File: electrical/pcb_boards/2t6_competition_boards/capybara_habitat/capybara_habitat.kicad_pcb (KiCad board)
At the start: 2 copper layers, 137.3 x 78 mm, 100 parts, among them J1 Barrel_Jack, J10 leds_sw, J11 monitor2_power, J12 2nd_disp_sw, J13 spare_usb_2nd_disp_pwr, J14 aud_sig_out_a, J15 aud_sig_out_b, J16 aud_sig_in, J18 spkrs_sw, J2 charger_buck_in, J3 vbatt, J4 Raspberry_Pi_4, J5 Raspberry_Pi_4, J7 1st_disp_sw, J8 leds_power, J9 monitor1_power, U1 Adafruit_INA219, U2 Adafruit_INA219, U3 LTC3114IFE-1_TRPBF, U4 LT8610ABEMSE-5-TRPBF, U5 TPS22810DBV, U6 TPS22810DBV, U7 TPS22810DBV, U8 TPS22810DBV, U9 PAM8406D

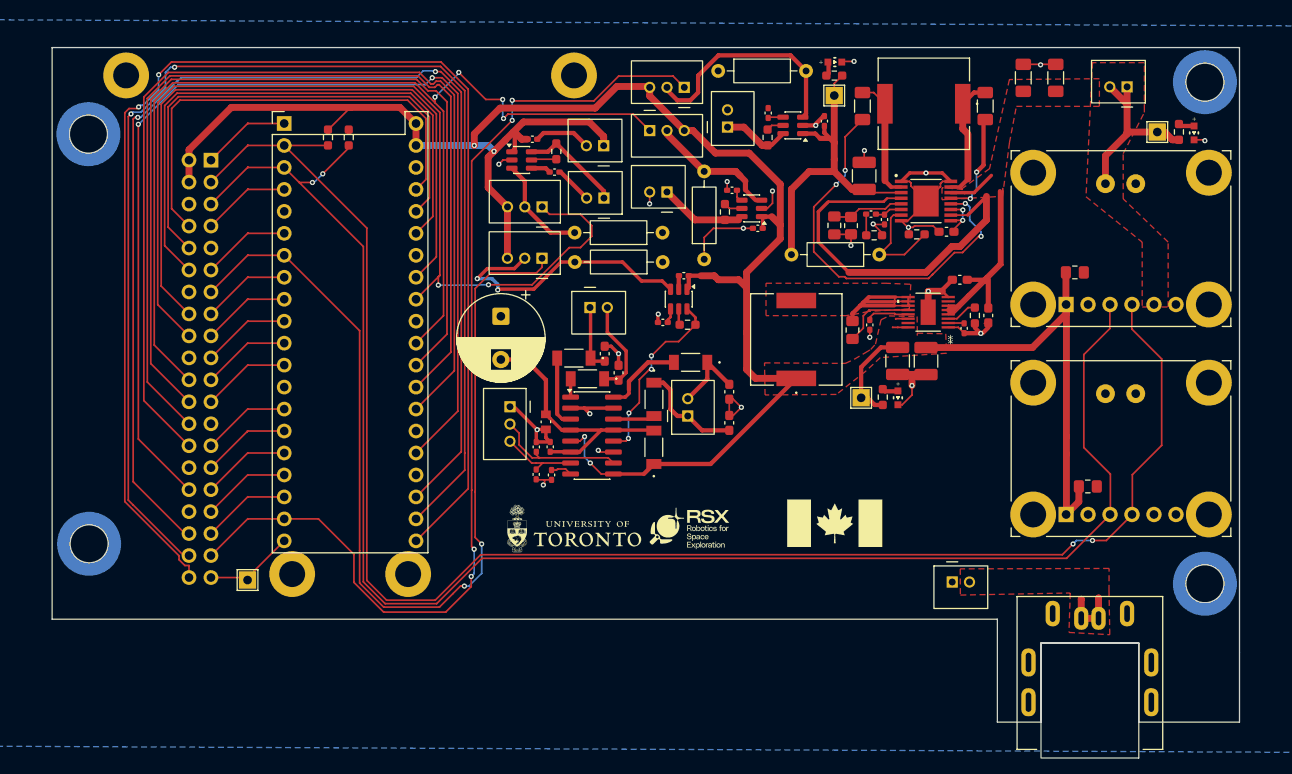
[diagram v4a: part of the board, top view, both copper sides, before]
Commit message: Fixed all GND trace issues
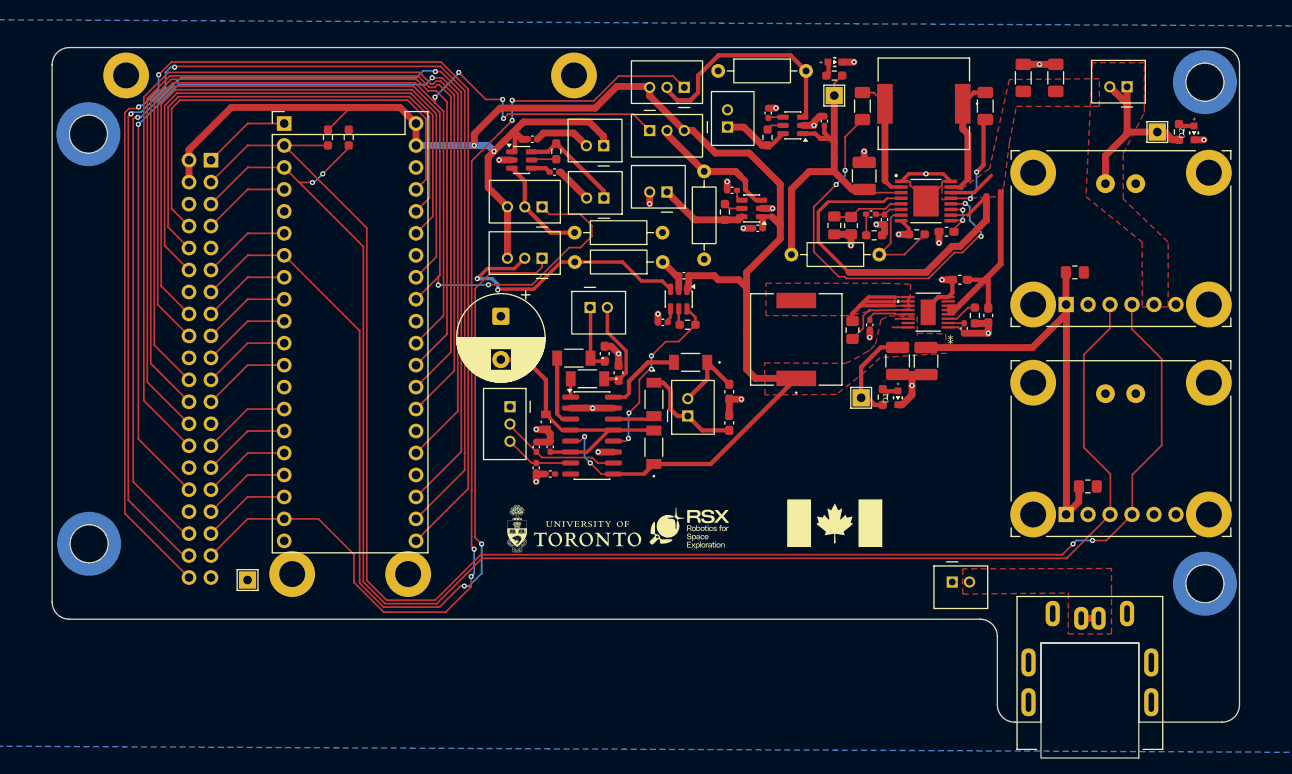
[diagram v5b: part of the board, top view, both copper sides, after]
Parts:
- moved D1 45.9 mm to (208.5, 105.5)
- moved D2 45.9 mm to (242.7, 74.9)
- moved C7 0.76 mm to (166.7, 113.6)
- moved C11 0.19 mm to (168.3, 114.3), turned to 180 degrees
- renumbered C13 to C1, C17 to C11, C19 to C12, C18 to C13, C20 to C14, C28 to C15, C29 to C16, C22 to C17, C23 to C18, C21 to C19, C25 to C2, C24 to C20, C31 to C21, C30 to C22, C7 to C23, C2 to C24, C33 to C25, C32 to C26, C1 to C27, C9 to C28, C34 to C29, C14 to C3, C6 to C30, C36 to C31, C3 to C32, C8 to C33, C35 to C34, C4 to C35, C5 to C36, C12 to C4, C15 to C5, C16 to C6, C26 to C7, C27 to C8, C11 to C9, J11 to J10, J14 to J11, J13 to J12, J12 to J13, J18 to J14, J4 to J15, J5 to J16, J8 to J2, J9 to J3, J2 to J4, J10 to J5, J7 to J6, J15 to J7, J3 to J8, J16 to J9, L7 to L1, L1 to L6, L6 to L7, R15 to R1, R25 to R10, R24 to R11, R16 to R12, R10 to R13, R11 to R14, R8 to R15, R2 to R16, R3 to R17, R1 to R18, R13 to R2, R12 to R3, R7 to R4, R4 to R5, R5 to R6, R9 to R7, R14 to R8, R6 to R9, TP2 to TP1, TP1 to TP2, TP4 to TP3, TP3 to TP4, U6 to U1, U7 to U2, U8 to U3, U1 to U4, U2 to U5, U9 to U6, U5 to U7, U4 to U8, U3 to U9
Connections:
- R1 pad 1: Net-(D2-A) -> Net-(D1-A)
- R4 pad 1: Net-(D1-A) -> Net-(D2-A)
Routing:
- net GND: track 133.4 -> 101.4 mm, vias 25 -> 27
- net Net-(J1-Pad1): track 6.59 -> 2.00 mm
- net Net-(U6-VREF): track 2.50 -> 0.00 mm
- net 5.0v: track 273.4 -> 274.9 mm
- net aud_in_right: track 15.5 -> 13.9 mm
- net Net-(U6-PVDDL): track 31.8 -> 33.2 mm
- net aud_in_left: track 9.13 -> 8.05 mm
- net Net-(U1-VOUT): track 9.62 -> 10.2 mm
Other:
- outline, holes or cut-outs redrawn

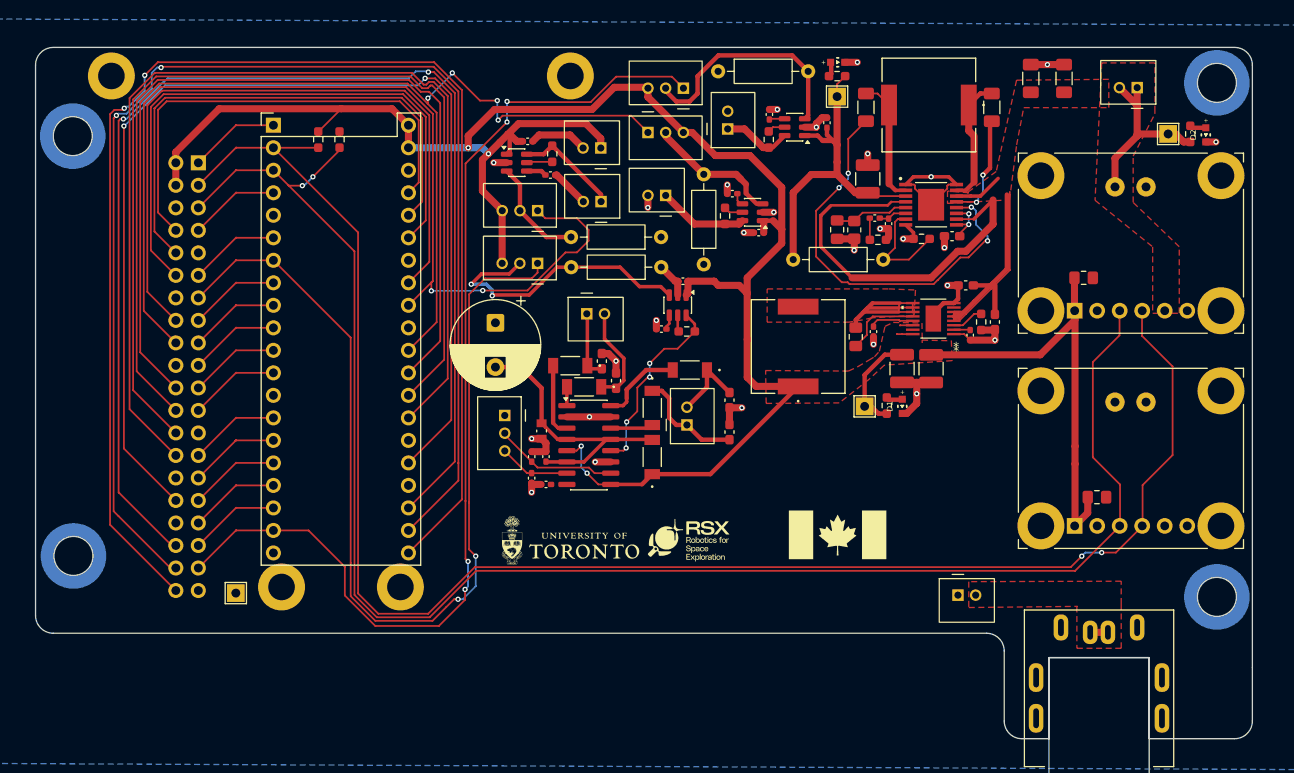
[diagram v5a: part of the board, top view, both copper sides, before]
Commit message: Adding new silkscreen graphics to ground station board
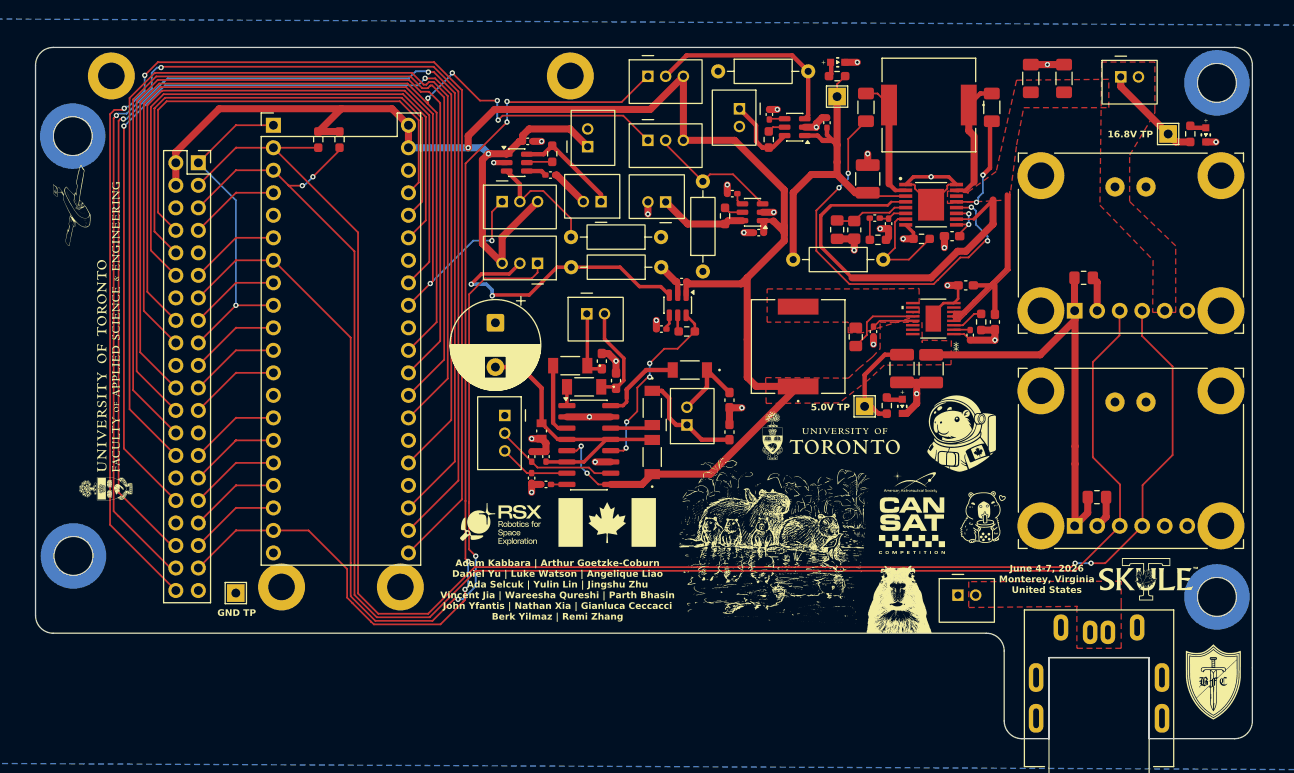
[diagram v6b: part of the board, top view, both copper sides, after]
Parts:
- added G***: LOGO, LOGO, F.Cu at (236.0, 125.0)
- added G***: LOGO, LOGO, F.Cu at (114.5, 82.8)
- added G***: LOGO, LOGO, B.Cu at (200.4, 77.2)
- added G***: LOGO, RSX_CanSat_Graphics:canada_flag, B.Cu at (214.2, 119.6)
- added G***: LOGO, RSX_CanSat_Graphics:rsx_new_logo, B.Cu at (214.2, 75.4)
- added G***: LOGO, RSX_CanSat_Graphics:capybara, B.Cu at (243.5, 135.9)
- added G***: LOGO, LOGO, B.Cu at (214.2, 87.6)
- added G***: LOGO, LOGO, B.Cu at (172.0, 98.7)
- added G***: LOGO, LOGO, B.Cu at (199.6, 119.8)
- added G***: LOGO, LOGO, F.Cu at (217.6, 118.0)
- added G***: LOGO, CAN-RGX:uoft, B.Cu at (214.2, 103.4)
- added G***: LOGO, LOGO, B.Cu at (232.7, 99.9)
- added G***: LOGO, LOGO, F.Cu at (215.2, 108.6)
- added G***: LOGO, LOGO, F.Cu at (193.8, 120.6)
- added G***: LOGO, RSX_CanSat_Graphics:capybara, F.Cu at (208.0, 126.6)
- added G***: LOGO, LOGO, F.Cu at (243.6, 136.6)
- added G***: LOGO, LOGO, F.Cu at (209.6, 117.4)
- added G***: LOGO, RSX_CanSat_Graphics:uoft_eng_logo, F.Cu at (118.6, 98.1)
- moved G*** 31.7 mm to (200.4, 109.0)
- moved G*** 26.0 mm to (175.2, 118.6)
- moved G*** 21.3 mm to (163.2, 118.8)
- moved J6 4.22 mm to (179.8, 68.3), turned to 0 degrees
- moved J13 4.14 mm to (163.3, 82.4), turned to 0 degrees
- moved J3 2.63 mm to (190.1, 71.9), turned to -90 degrees
- moved J8 2.21 mm to (233.2, 68.3), turned to 0 degrees
- moved J12 1.49 mm to (173.0, 76.2), turned to 90 degrees
- moved J5 0.89 mm to (179.8, 75.5)
- moved R6 0.81 mm to (186.0, 90.3)
- moved J2 0.74 mm to (181.8, 82.4)
- moved C15 0.16 mm to (183.6, 91.4)
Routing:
- net Net-(C31-Pad2): track 21.1 -> 0.10 mm
- net Net-(J15-3V3-Pad1): track 20.5 -> 38.3 mm, vias 0 -> 1
- net 16.8v: track 117.4 -> 101.9 mm
- net pi_2nd_disp: track 115.0 -> 100.0 mm
- net pi_1st_disp: track 119.5 -> 114.9 mm
- net Net-(U2-EN/UVLO): track 26.4 -> 23.3 mm
- net Net-(J1-Pad1): track 2.00 -> 0.00 mm
- net GND: track 101.4 -> 103.3 mm, vias 27 -> 28
- net Net-(U6-VREF): track 0.00 -> 1.79 mm
- net Net-(U3-EN/UVLO): track 12.1 -> 13.7 mm
- net Net-(U6-PVDDL): track 33.2 -> 31.8 mm
- net 12.0v: track 40.6 -> 39.8 mm
- net Net-(U2-VOUT): track 7.86 -> 8.53 mm
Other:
- board text added: "16.8V TP"
- board text added: "5.0V TP"
- board text added: "Adam Kabbara | Arthur Goetzke-Coburn Daniel Yu | Luke Watson | Angelique Liao Ada Selcuk | Yulin Lin | Jingshu Zhu Vincent Jia | Wareesha Qureshi | Parth Bhasin John Yfantis | Nathan Xia | Gianluca Ceccacci Berk Yilmaz | Remi Zhang"
- board text added: "GND TP"
- board text added: "June 4-7, 2026 Monterey, Virginia United States"
- board text removed: "${REFERENCE}"
